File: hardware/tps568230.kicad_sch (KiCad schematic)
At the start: 36 parts, among them U3 TPS568230, U4 LD39050PU33R

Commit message: Updating component placement
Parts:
- C10, C11, C12, C13, C5, C6, C9: footprint Capacitor_SMD:C_0805_2012Metric -> Capacitor_SMD:C_1206_3216Metric
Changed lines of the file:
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@@
 			)
 		)
-		(property "Footprint" "Capacitor_SMD:C_0805_2012Metric"
+		(property "Footprint" "Capacitor_SMD:C_1206_3216Metric"
 			(at 96.2152 43.18 0)
 			(effects
@@
 			)
 		)
-		(property "Footprint" "Capacitor_SMD:C_0805_2012Metric"
+		(property "Footprint" "Capacitor_SMD:C_1206_3216Metric"
 			(at 199.0852 55.88 0)
 			(effects
@@
 			)
 		)
-		(property "Footprint" "Capacitor_SMD:C_0805_2012Metric"
+		(property "Footprint" "Capacitor_SMD:C_1206_3216Metric"
 			(at 89.8652 43.18 0)
 			(effects
@@
 			)
 		)
-		(property "Footprint" "Capacitor_SMD:C_0805_2012Metric"
+		(property "Footprint" "Capacitor_SMD:C_1206_3216Metric"
 			(at 206.7052 55.88 0)
 			(effects
@@
 			)
 		)
-		(property "Footprint" "Capacitor_SMD:C_0805_2012Metric"
+		(property "Footprint" "Capacitor_SMD:C_1206_3216Metric"
 			(at 221.9452 55.88 0)
 			(effects
@@
 			)
 		)
-		(property "Footprint" "Capacitor_SMD:C_0805_2012Metric"
+		(property "Footprint" "Capacitor_SMD:C_1206_3216Metric"
 			(at 229.5652 55.88 0)
 			(effects
@@
 			)
 		)
-		(property "Footprint" "Capacitor_SMD:C_0805_2012Metric"
+		(property "Footprint" "Capacitor_SMD:C_1206_3216Metric"
 			(at 214.3252 55.88 0)
 			(effects

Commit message: adding inductor 3d model
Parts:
- L2: footprint Inductor_SMD:L_7.3x7.3_H3.5 -> Chromapi_FP:INDM6864X300N
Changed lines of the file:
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@@
 			)
 		)
-		(property "Footprint" "Inductor_SMD:L_7.3x7.3_H3.5"
+		(property "Footprint" "Chromapi_FP:INDM6864X300N"
 			(at 161.29 46.99 0)
 			(effects

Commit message: Applying first corrections from first review
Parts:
- U4: MP LD39050PU33R -> (none); MPN (none) -> LD39050PU33R
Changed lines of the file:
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@@
 		)
 	)
+	(text_box "4.5-18V Input, 8A\nFsw: 800kHz"
+		(exclude_from_sim no)
+		(at 139.7 66.04 0)
+		(size 21.59 6.35)
+		(margins 0.9525 0.9525 0.9525 0.9525)
+		(stroke
+			(width 0)
+			(type solid)
+		)
+		(fill
+			(type none)
+		)
+		(effects
+			(font
+				(size 1.27 1.27)
+			)
+			(justify top)
+		)
+	)
 	(text_box "5V to 3.3V Voltage Regulator"
 		(exclude_from_sim no)
@@
 		)
 	)
+	(text_box "1.5-5.5V Input, 500mA"
+		(exclude_from_sim no)
+		(at 189.23 142.24 0)
+		(size 25.4 3.81)
+		(margins 0.9525 0.9525 0.9525 0.9525)
+		(stroke
+			(width 0)
+			(type solid)
+		)
+		(fill
+			(type none)
+		)
+		(effects
+			(font
+				(size 1.27 1.27)
+			)
+			(justify top)
+		)
+	)
 	(text_box "7.2V to 5V Voltage Regulator"
 		(exclude_from_sim no)
@@
 					(size 1.27 1.27)
 				)
+				(hide yes)
 			)
 		)
@@
 					(size 1.27 1.27)
 				)
+				(hide yes)
 			)
 		)
@@
 					(size 1.27 1.27)
 				)
+				(hide yes)
 			)
 		)
@@
 					(size 1.27 1.27)
 				)
+				(hide yes)
 			)
 		)
@@
 					(size 1.27 1.27)
 				)
+				(hide yes)
 			)
 		)
@@
 					(size 1.27 1.27)
 				)
+				(hide yes)
 			)
 		)
@@
 			)
 		)
-		(property "MP" "LD39050PU33R"
+		(property "MPN" "LD39050PU33R"
 			(at 201.93 132.08 0)
 			(effects
@@
 					(size 1.27 1.27)
 				)
+				(hide yes)
 			)
 		)
@@
 					(size 1.27 1.27)
 				)
+				(hide yes)
 			)
 		)
@@
 					(size 1.27 1.27)
 				)
+				(hide yes)
 			)
 		)
@@
 					(size 1.27 1.27)
 				)
+				(hide yes)
 			)
 		)
@@
 					(size 1.27 1.27)
 				)
+				(hide yes)
 			)
 		)

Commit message: Updating schematic
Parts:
- D5: footprint LED_SMD:LED_0402_1005Metric -> LED_SMD:LED_0603_1608Metric; MPN (none) -> 150060SS55040
- D6: footprint LED_SMD:LED_0402_1005Metric -> LED_SMD:LED_0603_1608Metric; MPN (none) -> 150060GS55040
- D7: footprint LED_SMD:LED_0402_1005Metric -> LED_SMD:LED_0603_1608Metric; MPN (none) -> 150060BS55040
- R17: value 3.3k -> 2.7k
- R19: value 470 -> 560
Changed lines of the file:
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@@
 			)
 		)
-		(property "Value" "470"
+		(property "Value" "560"
 			(at 105.918 129.286 0)
 			(effects
@@
 			)
 		)
-		(property "Value" "3.3k"
+		(property "Value" "2.7k"
 			(at 75.184 129.286 0)
 			(effects
@@
 			)
 		)
-		(property "Footprint" "LED_SMD:LED_0402_1005Metric"
+		(property "Footprint" "LED_SMD:LED_0603_1608Metric"
 			(at 111.76 139.7 0)
 			(effects
@@
 			)
 		)
-		(property "Description" "Light emitting diode"
+		(property "Description" "Light emitting diode (Blue)"
 			(at 111.76 139.7 0)
 			(effects
@@
 			)
 		)
+		(property "MPN" "150060BS55040"
+			(at 111.76 139.7 90)
+			(effects
+				(font
+					(size 1.27 1.27)
+				)
+				(hide yes)
+			)
+		)
 		(property "Sim.Device" ""
 			(at 111.76 139.7 90)
@@
 			)
 		)
-		(property "Footprint" "LED_SMD:LED_0402_1005Metric"
+		(property "Footprint" "LED_SMD:LED_0603_1608Metric"
 			(at 96.52 139.7 0)
 			(effects
@@
 			)
 		)
-		(property "Description" "Light emitting diode"
+		(property "Description" "Light emitting diode (Green)"
 			(at 96.52 139.7 0)
 			(effects
@@
 			)
 		)
+		(property "MPN" "150060GS55040"
+			(at 96.52 139.7 90)
+			(effects
+				(font
+					(size 1.27 1.27)
+				)
+				(hide yes)
+			)
+		)
 		(property "Sim.Device" ""
 			(at 96.52 139.7 90)
@@
 			)
 		)
-		(property "Footprint" "LED_SMD:LED_0402_1005Metric"
+		(property "Footprint" "LED_SMD:LED_0603_1608Metric"
 			(at 81.28 139.7 0)
 			(effects
@@
 			)
 		)
-		(property "Description" "Light emitting diode"
+		(property "Description" "Light emitting diode (Red)"
 			(at 81.28 139.7 0)
 			(effects
@@
 			(effects
 				(font
+					(size 1.27 1.27)
+				)
+				(hide yes)
+			)
+		)
+		(property "MPN" "  150060SS55040"
+			(at 81.28 139.7 90)
+			(effects
+				(font

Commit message: IMU modification and Power monitor addition
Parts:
- renumbered C8 to C10, C9 to C11, C10 to C12, C11 to C13, C12 to C14, C13 to C15, C14 to C16, C15 to C17, C16 to C18, C17 to C19, C18 to C20, C19 to C21, C20 to C22, C5 to C7, C6 to C8, C7 to C9, R9 to R14, R10 to R15, R11 to R16, R12 to R17, R13 to R18, R14 to R19, R15 to R20, R16 to R21, R17 to R22, R18 to R23, R19 to R24, U3 to U4, U4 to U5
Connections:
- net V_BATT renamed V_SYS

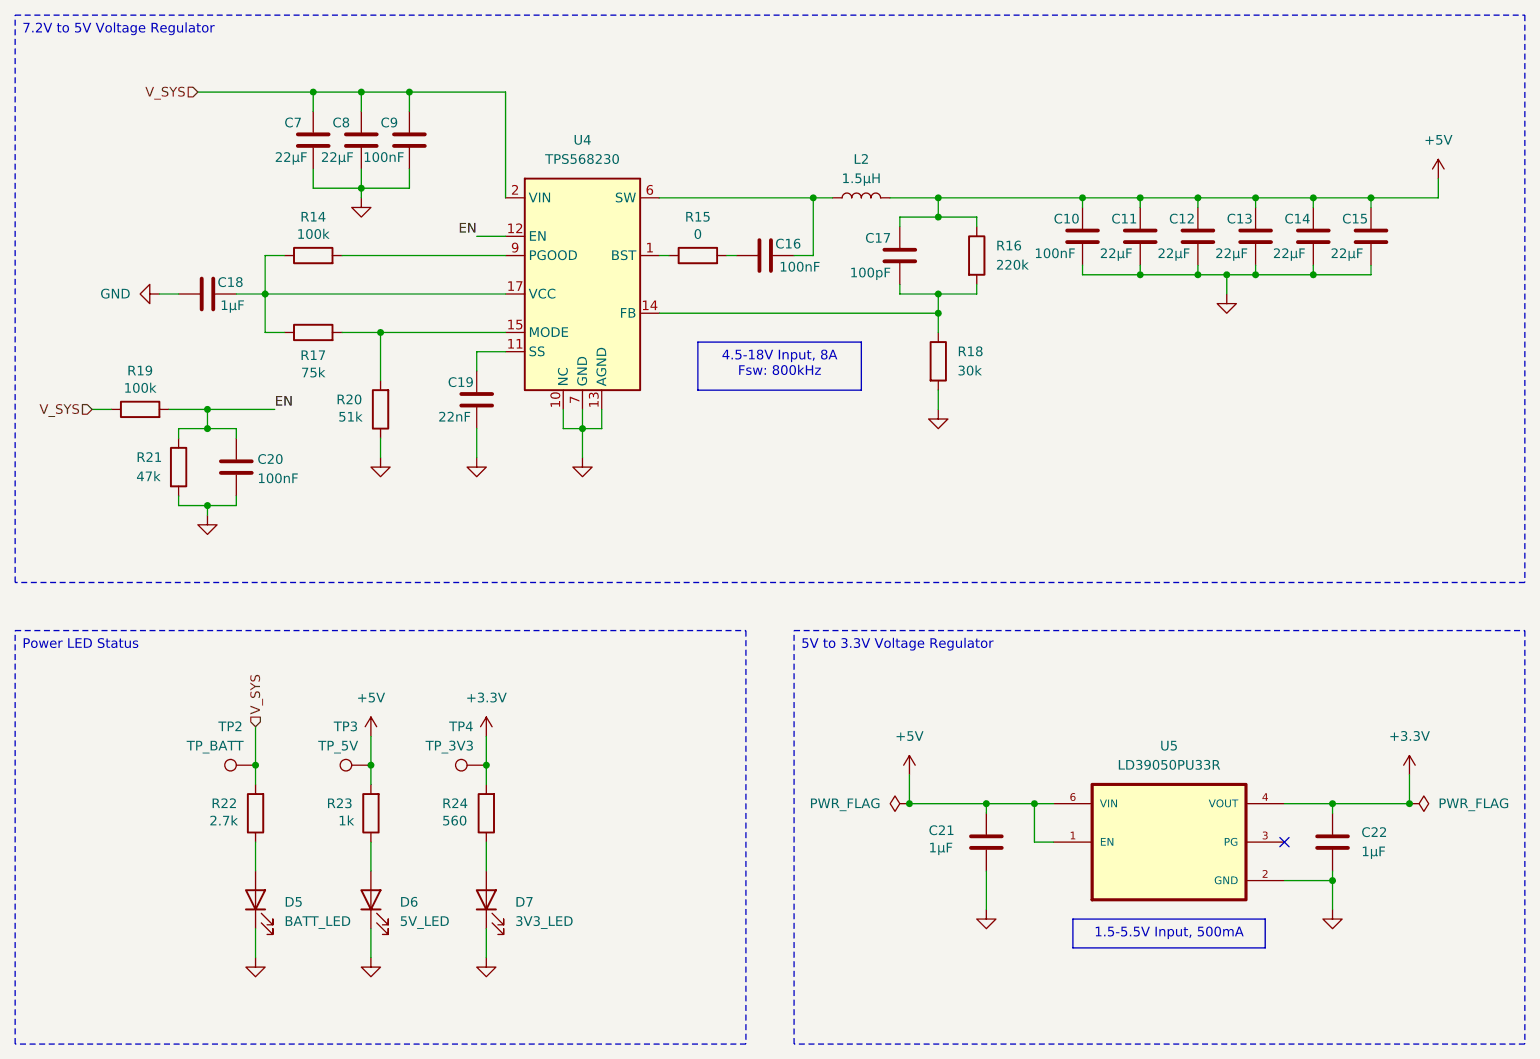
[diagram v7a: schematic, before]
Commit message: Upgrading voltage regulation circuit in schematic
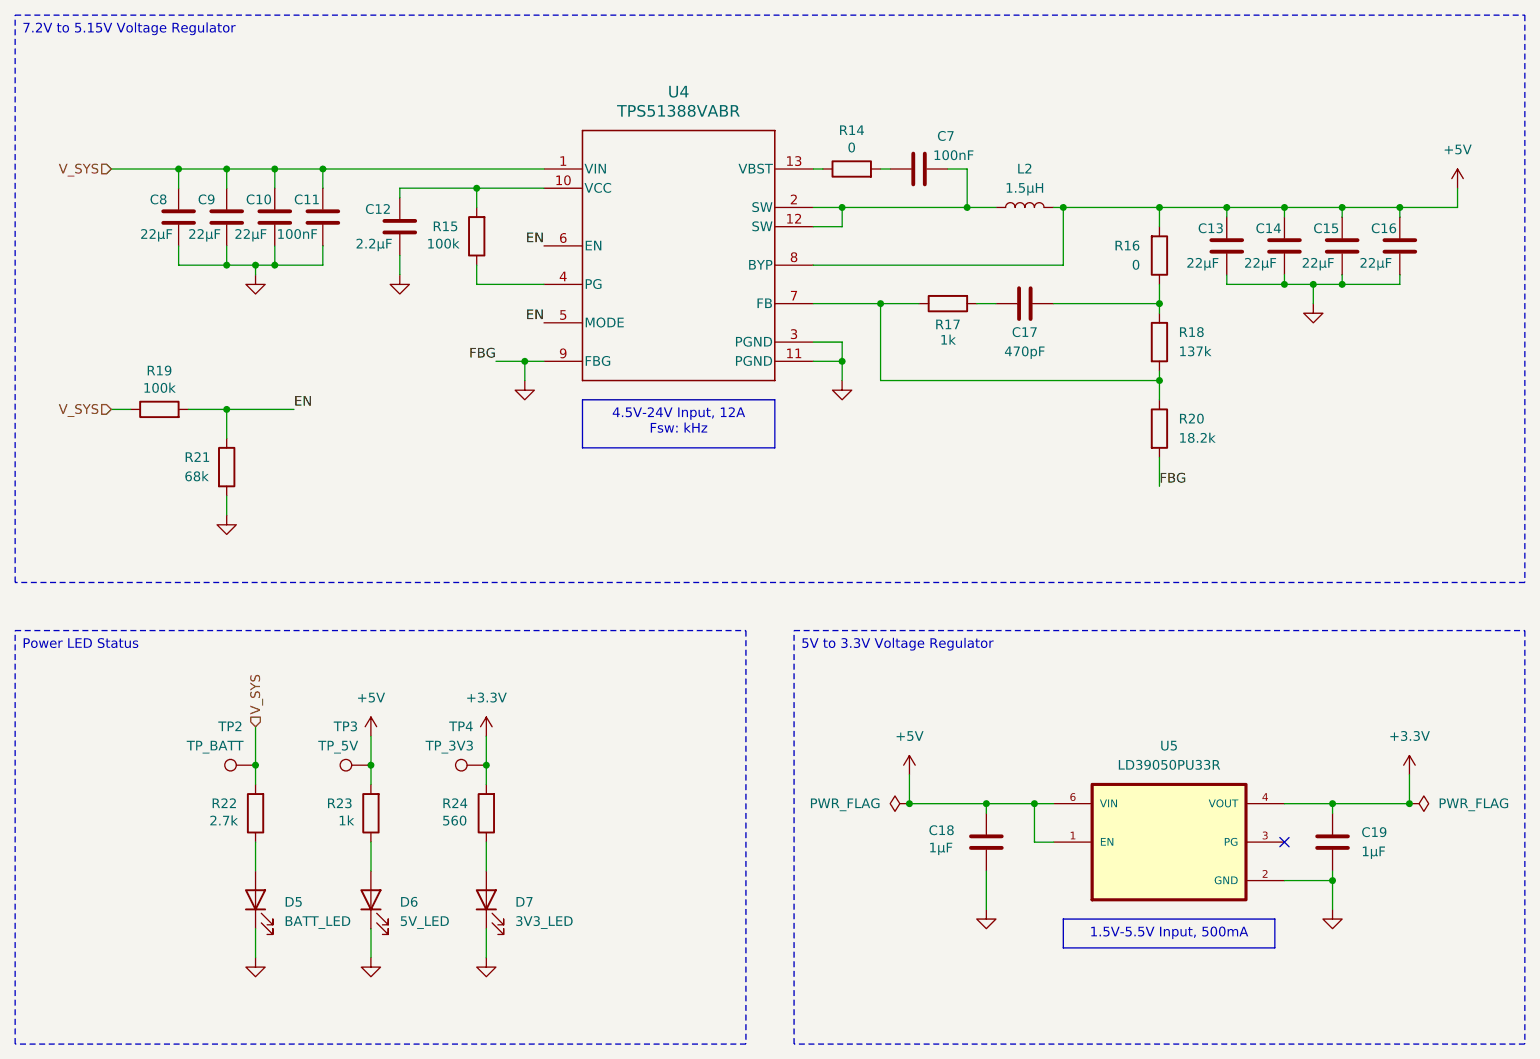
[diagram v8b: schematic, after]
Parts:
- removed C10: 100nF, Capacitor_SMD:C_0603_1608Metric, symbol Device:C
- removed C15: 22µF, Capacitor_SMD:C_1206_3216Metric, symbol Device:C
- removed C18: 1µF, Capacitor_SMD:C_0603_1608Metric, symbol Device:C
- removed C19: 22nF, Capacitor_SMD:C_0603_1608Metric, symbol Device:C
- removed C20: 100nF, Capacitor_SMD:C_0402_1005Metric, symbol Device:C
- removed R14: 100k, LED_SMD:LED_0603_1608Metric, symbol Device:R
- removed R20: 51k, Resistor_SMD:R_0603_1608Metric, symbol Device:R
- removed U4: TPS568230, Package_DFN_QFN:Texas_RJE0020A_VQFN-20-1EP_3x3mm_P0.45mm_EP0.675x0.76mm, symbol tps568230:TPS568230
- added C12: 2.2µF, Capacitor_SMD:C_0603_1608Metric, symbol Device:C
- added C8: 22µF, Capacitor_SMD:C_1206_3216Metric, symbol Device:C
- added R15: 100k, Resistor_SMD:R_0603_1608Metric, symbol Device:R
- added R16: 0, Resistor_SMD:R_0603_1608Metric, symbol Device:R
- added U4: TPS51388VABR, Chromapi_FP:VAB0013A-MFG, symbol tps51388:TPS51388VABR
- C13: renamed from C11; footprint Capacitor_SMD:C_1206_3216Metric -> Capacitor_SMD:C_0805_2012Metric
- C14: renamed from C12; footprint Capacitor_SMD:C_1206_3216Metric -> Capacitor_SMD:C_0805_2012Metric
- C15: renamed from C13; footprint Capacitor_SMD:C_1206_3216Metric -> Capacitor_SMD:C_0805_2012Metric
- C16: renamed from C14; footprint Capacitor_SMD:C_1206_3216Metric -> Capacitor_SMD:C_0805_2012Metric
- C17: value 100pF -> 470pF
- R17: value 75k -> 1k
- R18: renamed from R16; value 220k -> 137k
- R20: renamed from R18; value 30k -> 18.2k
- R21: value 47k -> 68k; footprint Resistor_SMD:R_0603_1608Metric -> Resistor_SMD:R_0402_1005Metric
- renumbered C8 to C10, C9 to C11, C21 to C18, C22 to C19, C16 to C7, C7 to C9, R15 to R14
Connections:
- net +5V: now also R16.2, U4.8 (BYP); no longer C17.1, R18.1
- net EN: now also U4.5 (MODE), U4.6 (EN)
- net GND: now also C12.2, C8.2, U4.11 (PGND), U4.3 (PGND), U4.9 (FBG)
- net V_SYS: now also C8.1, U4.1 (VIN)
- net at C7.1, L2.1: now also U4.12 (SW), U4.2 (SW)
- net at R17.1: now also R18.2, R20.1, U4.7 (FB)
- net at R17.2: now also C17.2
- net at R14.1: now also U4.13 (VBST)
- new net: C17.1, R16.1, R18.1
- new net: R15.1, U4.4 (PG)
- new net: C12.1, R15.2, U4.10 (VCC)
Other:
- moved on the sheet: C10, C11, C13, C14, C15, C16, C7, C9, L2, R14, R18, R19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
